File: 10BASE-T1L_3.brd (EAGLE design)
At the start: 60.8 x 75 mm, 172 parts, among them J1 10104110-0001LF, J2 A-2004-2-4-LPS-N-R, J3 KF141R-2.54-3P, J4 KF141R-2.54-2P, T1 ALT4532M-201-T001, T4 H1102NLT, U1 DP83TD510ERHBR, U2 DP83822IRHBR, U3 CO32H4-25.000-33GDTST, U4 LMR38020SDDAR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

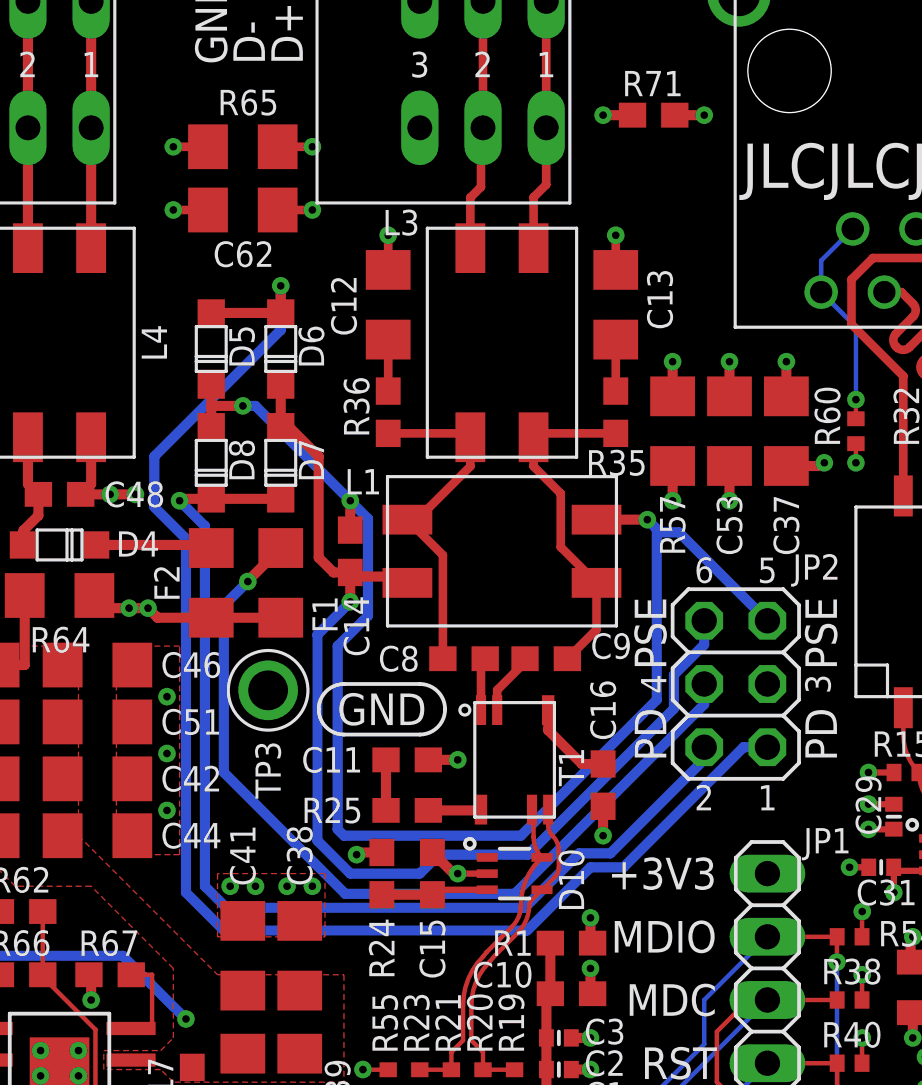
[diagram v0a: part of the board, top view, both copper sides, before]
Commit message: Adding V3 with inductor PoDL
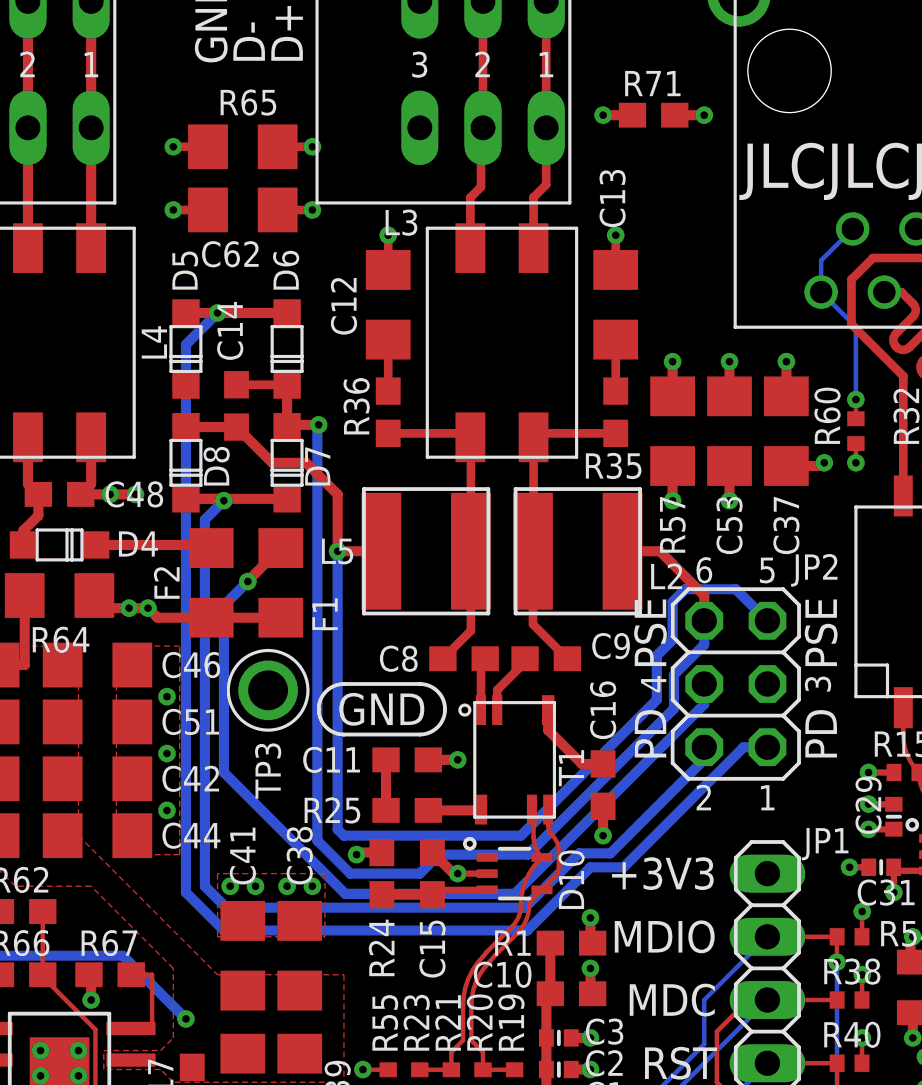
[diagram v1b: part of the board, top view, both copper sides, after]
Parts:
- removed L1: 1mH, ruark2:SMCM090605
- added L2, L5: 1mH, ruark2:SNR5040
- moved C14 7.42 mm to (18.3, 55.6), turned to 90 degrees
- moved D5 1.02 mm to (16.3, 57.9)
- moved D8 1.02 mm to (16.3, 53.3)
- moved D6 0.25 mm to (20.3, 57.9)
- moved D7 0.25 mm to (20.3, 53.3)
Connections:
- removed net N$17: C8.1, L1.IN2, L3.OUT1, R36.2
- removed net N$18: C9.2, L1.OUT1, L3.OUT2, R35.2
- new net IN+L: C9.2, L2.P$2, L3.OUT2, R35.2
- new net IN-L: C8.1, L3.OUT1, L5.P$2, R36.2
- net IN+: now also L2.P$1; no longer L1.IN1
- net IN-: now also L5.P$1; no longer L1.OUT2
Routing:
- net N$17: track 14.2 -> 0.00 mm
- net N$18: track 13.9 -> 0.00 mm
- net IN+L: track 0.00 -> 12.9 mm
- net IN-L: track 0.00 -> 12.8 mm
- net IN-: track 54.6 -> 46.4 mm, vias 3 -> 1
- net IN+: track 44.7 -> 48.8 mm
- net RTN: track 57.9 -> 54.9 mm
- net VIN: track 43.4 -> 44.8 mm
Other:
- board text added: "063"
- board text removed: "060"

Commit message: V3 Updates
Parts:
- R68: value 22k -> 51k
- R69: value 51k -> 22k
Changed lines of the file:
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@@
 <attribute name="VALUE" x="11.684" y="11.176" size="1.27" layer="27"/>
 </element>
-<element name="R68" library="ruark2" package="0603" value="22k" x="5.842" y="31.496" smashed="yes" rot="R90">
+<element name="R68" library="ruark2" package="0603" value="51k" x="5.842" y="31.496" smashed="yes" rot="R90">
 <attribute name="NAME" x="5.08" y="30.226" size="1.016" layer="25" font="vector" ratio="10" rot="R90"/>
 <attribute name="VALUE" x="7.62" y="30.226" size="1.016" layer="27" font="vector" rot="R90"/>
 </element>
-<element name="R69" library="ruark2" package="0603" value="51k" x="5.842" y="34.798" smashed="yes" rot="R270">
+<element name="R69" library="ruark2" package="0603" value="22k" x="5.842" y="34.798" smashed="yes" rot="R270">
 <attribute name="NAME" x="5.08" y="33.782" size="1.016" layer="25" font="vector" ratio="10" rot="R90"/>
 <attribute name="VALUE" x="4.064" y="36.068" size="1.016" layer="27" font="vector" rot="R270"/>
